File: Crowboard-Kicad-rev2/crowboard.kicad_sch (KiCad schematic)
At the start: 77 parts, among them J1 Conn_01x05, J2 Conn_01x04, SW1 RotaryEncoder, SW2 RotaryEncoder, U1 Pico

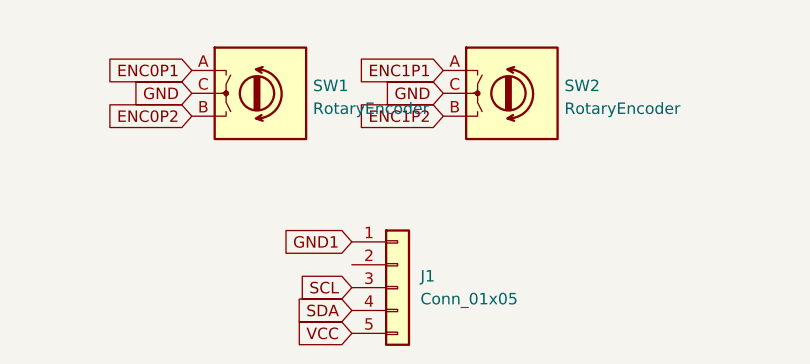
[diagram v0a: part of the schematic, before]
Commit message: Removed Pimoroni Trackball
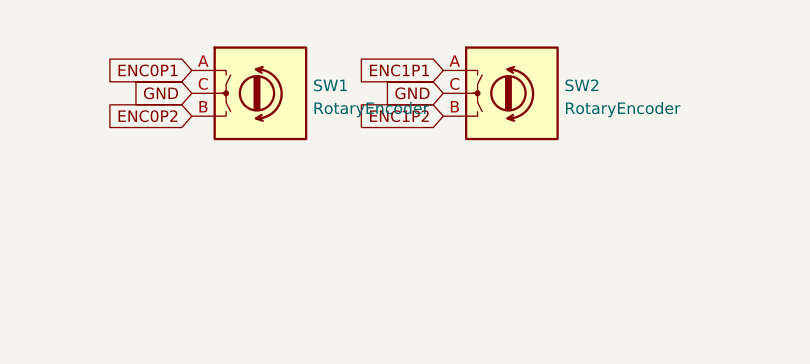
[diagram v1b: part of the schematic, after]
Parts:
- removed J1: Conn_01x05, other_parts:pimoroni, symbol Connector_Generic:Conn_01x05
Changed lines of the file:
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@@
-    )
-  )
-  (global_label "VCC" (shape input) (at 116.84 162.56 180) (fields_autoplaced)
-    (effects (font (size 1.27 1.27)) (justify right))
-    (property "Intersheet References" "${INTERSHEET_REFS}" (id 0) (at 110.7983 162.4806 0)
-      (effects (font (size 1.27 1.27)) (justify right) hide)
     )
   )
@@
     )
   )
-  (global_label "GND1" (shape input) (at 116.84 152.4 180) (fields_autoplaced)
-    (effects (font (size 1.27 1.27)) (justify right))
-    (property "Intersheet References" "${INTERSHEET_REFS}" (id 0) (at 109.3469 152.4794 0)
-      (effects (font (size 1.27 1.27)) (justify right) hide)
-    )
-  )
   (global_label "ROW1" (shape input) (at 40.64 120.65 180) (fields_autoplaced)
     (effects (font (size 1.27 1.27)) (justify right))
@@
     )
   )
-  (global_label "SDA" (shape input) (at 116.84 160.02 180) (fields_autoplaced)
-    (effects (font (size 1.27 1.27)) (justify right))
-    (property "Intersheet References" "${INTERSHEET_REFS}" (id 0) (at 110.8588 159.9406 0)
-      (effects (font (size 1.27 1.27)) (justify right) hide)
-    )
-  )
   (global_label "ENC1P1" (shape input) (at 127 133.35 180) (fields_autoplaced)
     (effects (font (size 1.27 1.27)) (justify right))
@@
     )
   )
-  (global_label "SCL" (shape input) (at 116.84 157.48 180) (fields_autoplaced)
-    (effects (font (size 1.27 1.27)) (justify right))
-    (property "Intersheet References" "${INTERSHEET_REFS}" (id 0) (at 110.9193 157.4006 0)
-      (effects (font (size 1.27 1.27)) (justify right) hide)
-    )
-  )
   (global_label "COL7" (shape input) (at 219.71 43.18 90) (fields_autoplaced)
     (effects (font (size 1.27 1.27)) (justify left))
@@
     (pin "1")
     (pin "2")
-  )
-  (symbol (lib_id "Connector_Generic:Conn_01x05") (at 121.92 157.48 0) (unit 1)
-    (in_bom yes) (on_board yes) (fields_autoplaced)
-    (property "Reference" "J1" (id 0) (at 124.46 156.2099 0)
-      (effects (font (size 1.27 1.27)) (justify left))
-    )
-    (property "Value" "Conn_01x05" (id 1) (at 124.46 158.7499 0)
-      (effects (font (size 1.27 1.27)) (justify left))
-    )
-    (property "Footprint" "other_parts:pimoroni" (id 2) (at 121.92 157.48 0)
-      (effects (font (size 1.27 1.27)) hide)
-    )
-    (property "Datasheet" "~" (id 3) (at 121.92 157.48 0)
-      (effects (font (size 1.27 1.27)) hide)
-    )
-    (pin "1")
-    (pin "2")
-    (pin "3")
-    (pin "4")
-    (pin "5")
   )
   (symbol (lib_id "Device:D_Small") (at 201.93 96.52 90) (unit 1)
@@
       (reference "D36") (unit 1) (value "D_Small") (footprint "Keebio-Parts:Diode-Hybrid-Back")
     )
-    (path "/117711d1-66af-4438-9393-903c3c375726"
-      (reference "J1") (unit 1) (value "Conn_01x05") (footprint "other_parts:pimoroni")
-    )
     (path "/1f095f88-a709-4dce-b0ed-23ea45ee11aa"
